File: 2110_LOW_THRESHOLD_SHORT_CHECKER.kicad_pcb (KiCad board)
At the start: 2 copper layers, 60 x 64 mm, 28 parts, among them CN2 2PIN, IC11 AD823AN, SW1 SS12D01G4

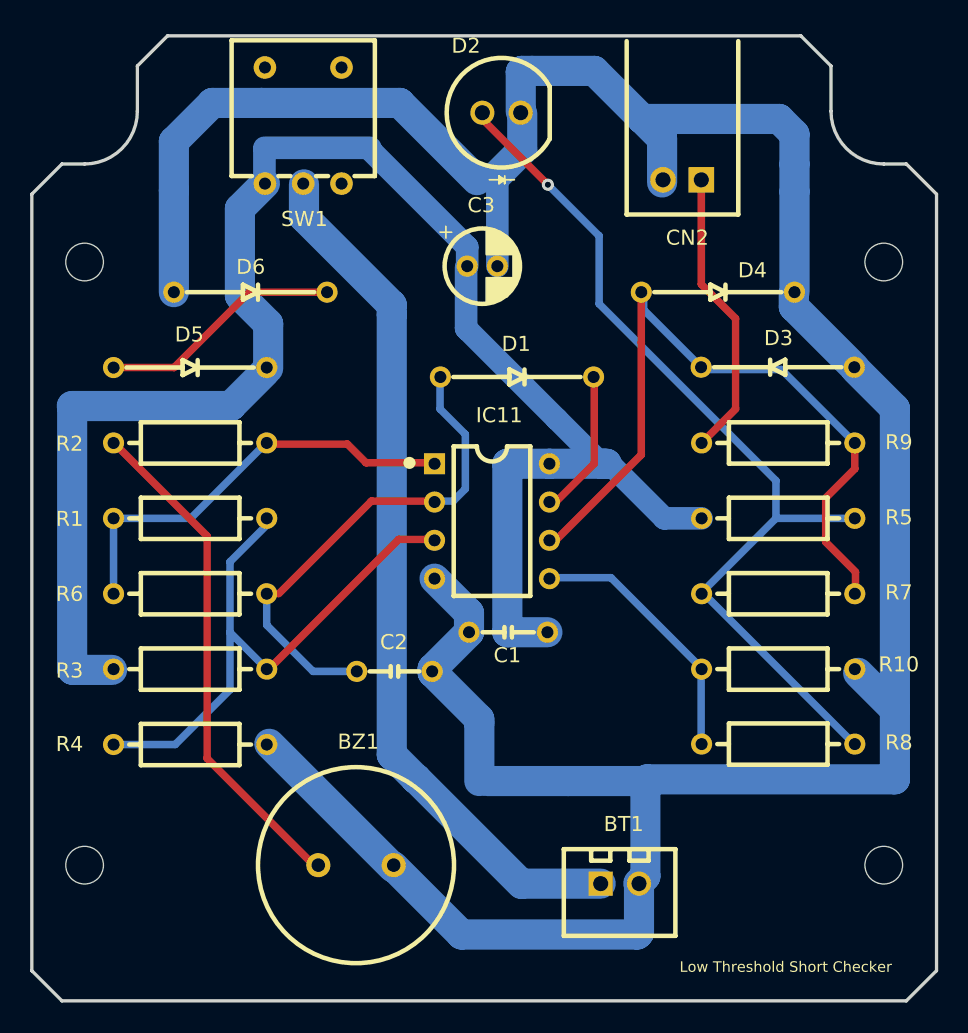
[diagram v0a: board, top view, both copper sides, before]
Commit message: 一部回路と、パターンの修正。
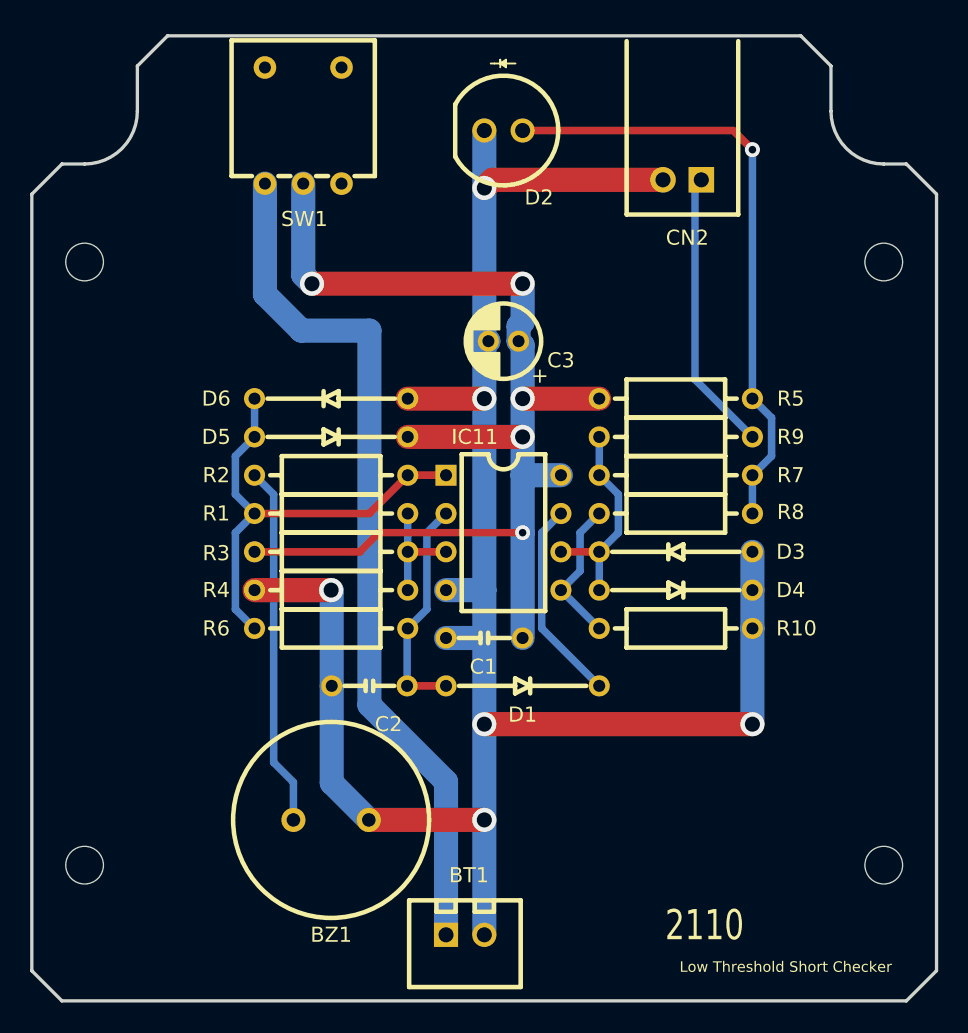
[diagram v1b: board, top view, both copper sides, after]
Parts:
- IC11: footprint AD823AN:AD823AN -> footprint:ic_DIP-8_W7.62mm
- moved D1 20.5 mm to (146.1, 118.1)
- moved D4 20.0 mm to (156.2, 111.8)
- moved R8 16.7 mm to (156.2, 106.7)
- moved D3 14.0 mm to (156.2, 109.2)
- moved R4 13.9 mm to (133.3, 111.8), turned to 180 degrees
- moved R3 12.2 mm to (133.3, 109.2)
- moved BT1 10.8 mm to (142.4, 134.6)
- moved R5 10.4 mm to (156.2, 99.1)
- moved D5 10.4 mm to (133.3, 101.6)
- moved R7 10.4 mm to (156.2, 104.1), turned to 180 degrees
- moved R6 9.63 mm to (133.3, 114.3)
- moved R2 9.59 mm to (133.3, 104.1)
- moved R1 9.36 mm to (133.3, 106.7)
- moved D6 8.86 mm to (133.3, 99.1), turned to 180 degrees
- moved R10 7.31 mm to (156.2, 114.3)
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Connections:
- IC11 pad 1: Net-(IC11-Pad1) -> Net-(D5-Pad1)
- R1 pad 1: Net-(IC11-Pad1) -> Net-(D5-Pad1)
- R2 pad 2: Net-(IC11-Pad1) -> Net-(D5-Pad1)
- R6 pad 1: Net-(IC11-Pad1) -> Net-(D5-Pad1)
- SW1 pad 1: +9V -> Net-(BT1-Pad1)
- SW1 pad 2: Net-(BT1-Pad1) -> +9V
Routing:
- net GND: track 206.3 -> 134.0 mm, vias 0 -> 6
- net Net-(D3-Pad2): track 49.4 -> 13.8 mm
- net +9V: track 112.4 -> 78.1 mm, vias 0 -> 5
- net Net-(IC11-Pad3): track 39.8 -> 7.62 mm
- net Net-(IC11-Pad1): track 28.6 -> 0.00 mm
- net Net-(D2-Pad1): track 60.7 -> 40.9 mm
- net Net-(C2-Pad1): track 33.2 -> 15.1 mm
- net Net-(D5-Pad1): track 16.2 -> 31.1 mm
- net Net-(BZ1-Pad1): track 34.2 -> 23.9 mm
- net Net-(IC11-Pad5): track 16.9 -> 9.72 mm
- net Net-(D1-Pad2): track 9.31 -> 13.5 mm
- net Net-(CN2-Pad1): track 19.4 -> 18.8 mm
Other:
- board text added: "2110"
